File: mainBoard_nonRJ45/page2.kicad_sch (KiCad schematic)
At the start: 33 parts, among them IC1 TCAN3414DR, J10 XT30U-M, J11 XT30U-M, J12 Conn_01x03, J13 BM02B-SRSS-TB, J14 BM02B-SRSS-TB, J15 BM02B-SRSS-TB, J16 BM04B-SRSS-TB, J17 BM04B-SRSS-TB, J18 BM04B-SRSS-TB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

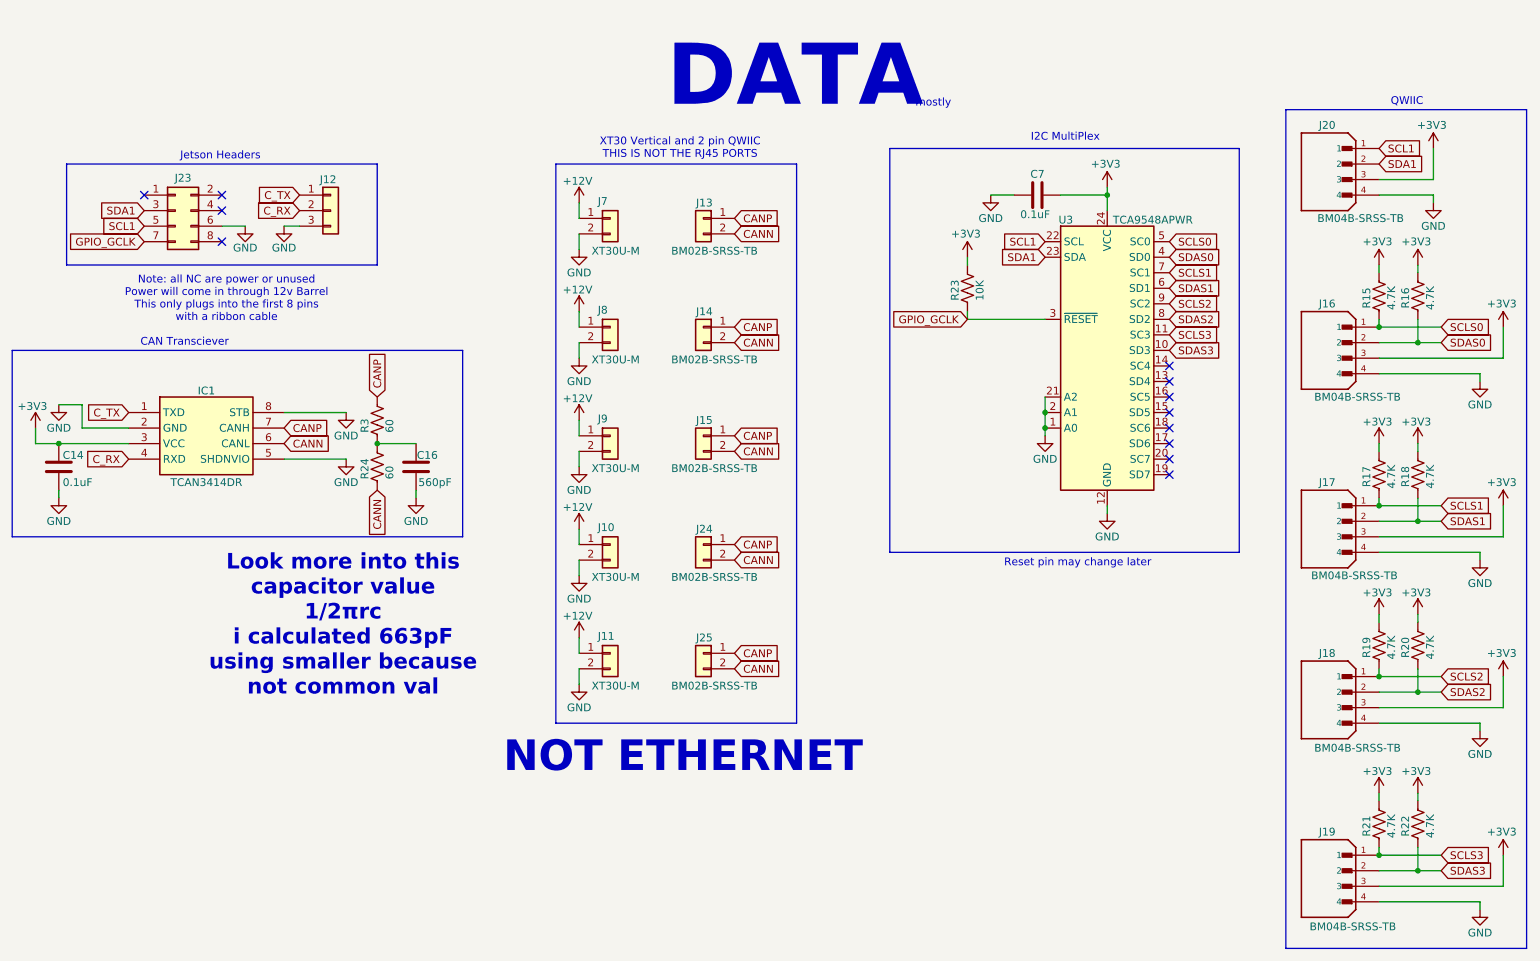
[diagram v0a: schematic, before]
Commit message: Reviewed PCB with justin and made changes
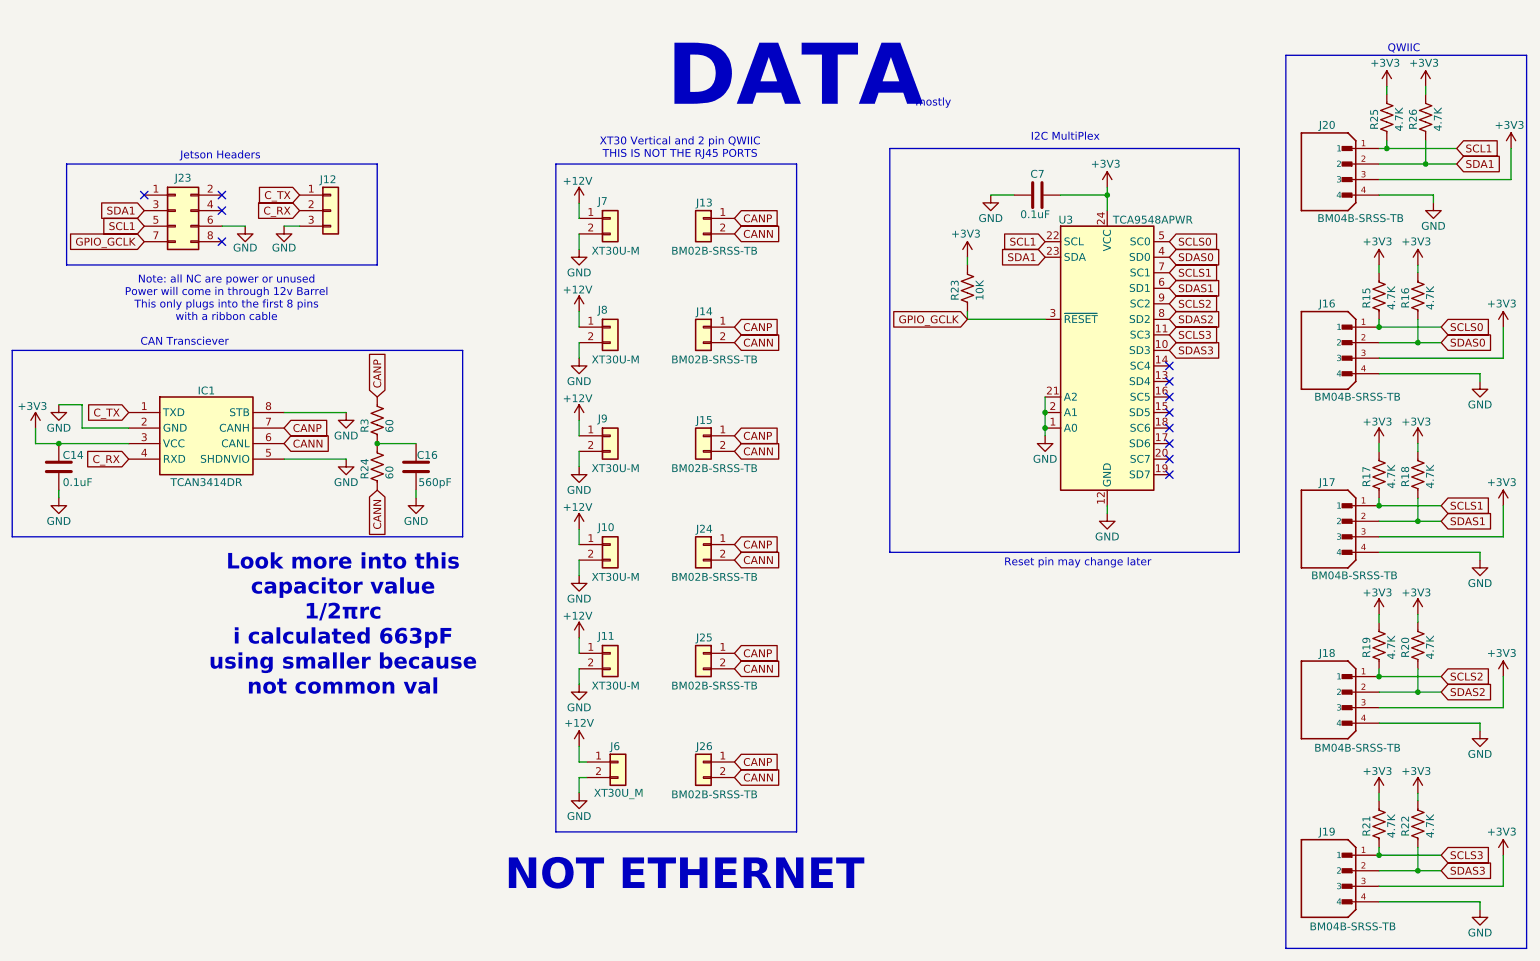
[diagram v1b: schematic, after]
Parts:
- added J26: BM02B-SRSS-TB, Connector_JST:JST_SH_BM02B-SRSS-TB_1x02-1MP_P1.00mm_Vertical, symbol Connector_Generic:Conn_01x02
- added J6: XT30U_M, Connector_AMASS:AMASS_XT30U-M_1x02_P5.0mm_Vertical, symbol Connector_Generic:Conn_01x02
- added R25, R26: 4.7K, Resistor_SMD:R_0805_2012Metric_Pad1.20x1.40mm_HandSolder, symbol Device:R_US
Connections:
- net +12V: now also J6.1 (Pin_1)
- net +3V3: now also R25.1, R26.1
- net CANN: now also J26.2 (Pin_2)
- net CANP: now also J26.1 (Pin_1)
- net GND: now also J6.2 (Pin_2)
- net SCL1: now also R25.2
- net SDA1: now also R26.2
